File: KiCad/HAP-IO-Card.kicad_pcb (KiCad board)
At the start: 2 copper layers, 110 x 72 mm, 424 parts, among them CON601 AVR-JTAG-10, J201 TE_Connectivity_1-282834-0, J202 TE_Connectivity_282834-6, J203 GS3, J204 GS3, J205 GS3, J206 GS3, J207 GS3, J208 GS3, J209 GS3, J210 GS3, J211 TE_Connectivity_282834-6, J212 TE_Connectivity_1-282834-0, J401 TE_Connectivity_1-282834-0, J402 TE_Connectivity_282834-6, J501 TE_Connectivity_282834-3, J502 CONN_01X03_FEMALE, J601 ISP0, J602 ISP1, J603 CONN_01X02, J604 CONN_01X02, J605 CONN_01X02, J606 CONN_01X02, J607 CONN_01X03, J608 CONN_01X03, J701 5V_I/O_1, J702 5V_I/O_2, J703 NEO1, J704 NEO2, J705 NEO3, J706 NEO4, J707 CONN_01X03, Q201 ZXTN25050DFHTA, Q202 ZXTN25050DFHTA, Q203 ZXTN25050DFHTA, Q204 ZXTN25050DFHTA, Q205 ZXTN25050DFHTA, Q206 ZXTN25050DFHTA, Q207 ZXTN25050DFHTA, Q208 ZXTN25050DFHTA, U201 LTV-354T, U202 LTV-354T, U203 LTV-354T, U204 LTV-354T, U205 LTV-354T, U206 LTV-354T, U207 LTV-354T, U208 LTV-354T, U209 MCP23017, U401 ADS1115IDGST, U402 ADS1115IDGST, U501 LM1086-5V, U502 LM1086-3.3V, U701 TXB0102DCT

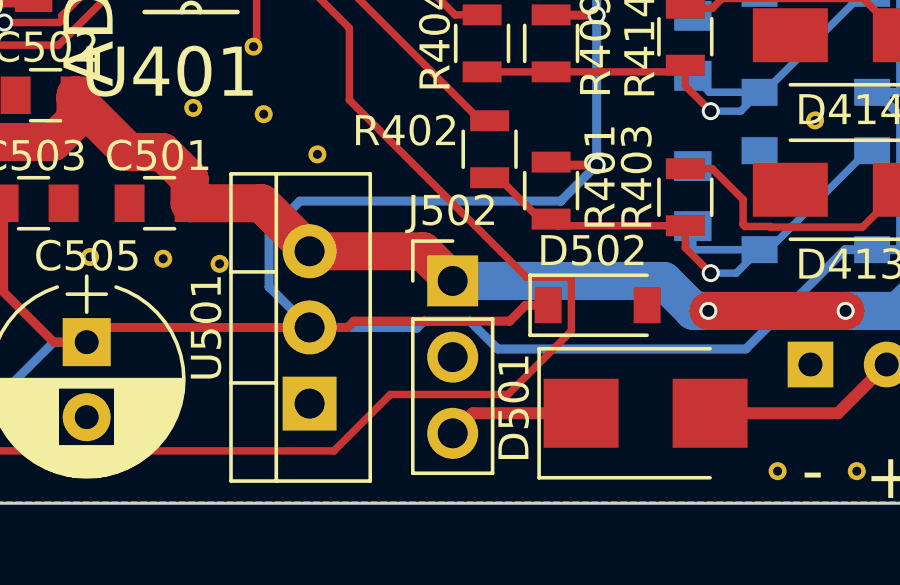
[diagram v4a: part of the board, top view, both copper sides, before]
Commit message: Updated EMI component
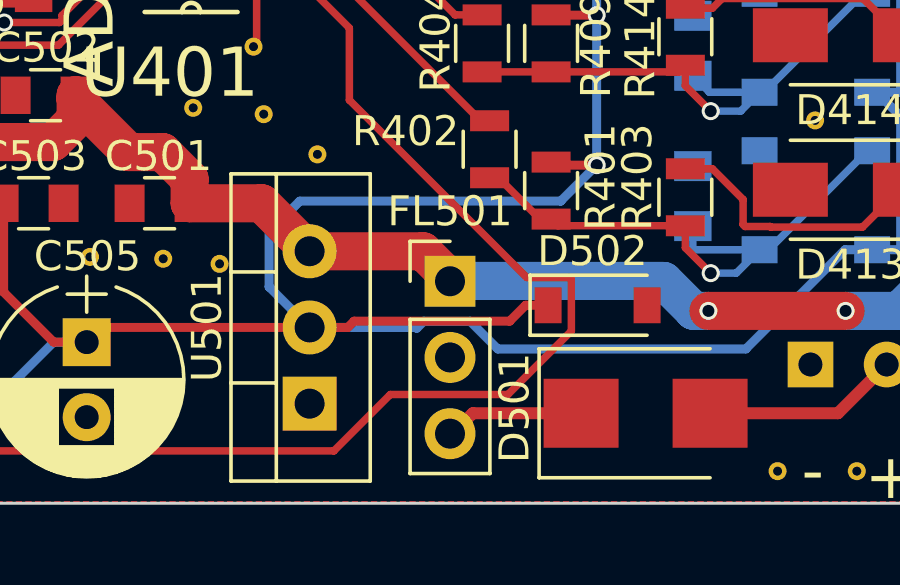
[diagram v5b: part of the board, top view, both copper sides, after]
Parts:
- removed J502: CONN_01X03_FEMALE, Pin_Headers:Pin_Header_Straight_1x03_Pitch2.54mm
- added FL501: EMI_Filter_LCL, Pin_Headers:Pin_Header_Straight_1x03_Pitch2.54mm, F.Cu at (119.9, 82.1)
- D501: value MBR340 -> MBRS360BT3G
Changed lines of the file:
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@@
     (add_net "/Sense Inputs/Sense8_DUT")
   )
+  (module Pin_Headers:Pin_Header_Straight_1x03_Pitch2.54mm (layer F.Cu)
+    (at 119.91 82.07)
+    (descr "Through hole straight pin header, 1x03, 2.54mm pitch, single row")
+    (tags "Through hole pin header THT 1x03 2.54mm single row")
+    (fp_text reference FL501 (at 0 -2.33) (layer F.SilkS)
+      (effects (font (size 1 1) (thickness 0.15)))
+    )
+    (fp_text value EMI_Filter_LCL (at 0 7.41) (layer F.Fab)
+      (effects (font (size 1 1) (thickness 0.15)))
+    )
+    (fp_text user %R (at 0 -2.33) (layer F.Fab)
+      (effects (font (size 1 1) (thickness 0.15)))
+    )
+    (fp_line (start 1.8 -1.8) (end -1.8 -1.8) (layer F.CrtYd) (width 0.05))
+    (fp_line (start 1.8 6.85) (end 1.8 -1.8) (layer F.CrtYd) (width 0.05))
+    (fp_line (start -1.8 6.85) (end 1.8 6.85) (layer F.CrtYd) (width 0.05))
+    (fp_line (start -1.8 -1.8) (end -1.8 6.85) (layer F.CrtYd) (width 0.05))
+    (fp_line (start -1.33 -1.33) (end 0 -1.33) (layer F.SilkS) (width 0.12))
+    (fp_line (start -1.33 0) (end -1.33 -1.33) (layer F.SilkS) (width 0.12))
+    (fp_line (start 1.33 1.27) (end -1.33 1.27) (layer F.SilkS) (width 0.12))
+    (fp_line (start 1.33 6.41) (end 1.33 1.27) (layer F.SilkS) (width 0.12))
+    (fp_line (start -1.33 6.41) (end 1.33 6.41) (layer F.SilkS) (width 0.12))
+    (fp_line (start -1.33 1.27) (end -1.33 6.41) (layer F.SilkS) (width 0.12))
+    (fp_line (start 1.27 -1.27) (end -1.27 -1.27) (layer F.Fab) (width 0.1))
+    (fp_line (start 1.27 6.35) (end 1.27 -1.27) (layer F.Fab) (width 0.1))
+    (fp_line (start -1.27 6.35) (end 1.27 6.35) (layer F.Fab) (width 0.1))
+    (fp_line (start -1.27 -1.27) (end -1.27 6.35) (layer F.Fab) (width 0.1))
+    (pad 3 thru_hole oval (at 0 5.08) (size 1.7 1.7) (drill 1) (layers *.Cu *.Mask)
+      (net 157 /Powersupply/12V_PWR2))
+    (pad 2 thru_hole oval (at 0 2.54) (size 1.7 1.7) (drill 1) (layers *.Cu *.Mask)
+      (net 94 Earth))
+    (pad 1 thru_hole rect (at 0 0) (size 1.7 1.7) (drill 1) (layers *.Cu *.Mask)
+      (net 107 +12V))
+    (model ${KISYS3DMOD}/Pin_Headers.3dshapes/Pin_Header_Straight_1x03_Pitch2.54mm.wrl
+      (at (xyz 0 -0.1 0))
+      (scale (xyz 1 1 1))
+      (rotate (xyz 0 0 90))
+    )
+  )
   (module Resistors_SMD:R_0805 (layer B.Cu)
     (at 87.67 86 270)
@@
       (effects (font (size 1 1) (thickness 0.15)))
     )
-    (fp_text value MBR340 (at 0 3.1) (layer F.Fab)
+    (fp_text value MBRS360BT3G (at 0 3.1) (layer F.Fab)
       (effects (font (size 1 1) (thickness 0.15)))
     )
@@
     (model ${KISYS3DMOD}/Pin_Headers.3dshapes/Pin_Header_Straight_1x03_Pitch2.54mm.wrl
       (at (xyz 0 -0.1 0))
-      (scale (xyz 1 1 1))
-      (rotate (xyz 0 0 90))
-    )
-  )
-  (module Pin_Headers:Pin_Header_Straight_1x03_Pitch2.54mm (layer F.Cu)
-    (at 120 82.06)
-    (descr "Through hole straight pin header, 1x03, 2.54mm pitch, single row")
-    (tags "Through hole pin header THT 1x03 2.54mm single row")
-    (fp_text reference J502 (at 0 -2.33) (layer F.SilkS)
-      (effects (font (size 1 1) (thickness 0.15)))
-    )
-    (fp_text value CONN_01X03_FEMALE (at 0 7.41) (layer F.Fab)
-      (effects (font (size 1 1) (thickness 0.15)))
-    )
-    (fp_text user %R (at 0 -2.33) (layer F.Fab)
-      (effects (font (size 1 1) (thickness 0.15)))
-    )
-    (fp_line (start 1.8 -1.8) (end -1.8 -1.8) (layer F.CrtYd) (width 0.05))
-    (fp_line (start 1.8 6.85) (end 1.8 -1.8) (layer F.CrtYd) (width 0.05))
-    (fp_line (start -1.8 6.85) (end 1.8 6.85) (layer F.CrtYd) (width 0.05))
-    (fp_line (start -1.8 -1.8) (end -1.8 6.85) (layer F.CrtYd) (width 0.05))
-    (fp_line (start -1.33 -1.33) (end 0 -1.33) (layer F.SilkS) (width 0.12))
-    (fp_line (start -1.33 0) (end -1.33 -1.33) (layer F.SilkS) (width 0.12))
-    (fp_line (start 1.33 1.27) (end -1.33 1.27) (layer F.SilkS) (width 0.12))
-    (fp_line (start 1.33 6.41) (end 1.33 1.27) (layer F.SilkS) (width 0.12))
-    (fp_line (start -1.33 6.41) (end 1.33 6.41) (layer F.SilkS) (width 0.12))
-    (fp_line (start -1.33 1.27) (end -1.33 6.41) (layer F.SilkS) (width 0.12))
-    (fp_line (start 1.27 -1.27) (end -1.27 -1.27) (layer F.Fab) (width 0.1))
-    (fp_line (start 1.27 6.35) (end 1.27 -1.27) (layer F.Fab) (width 0.1))
-    (fp_line (start -1.27 6.35) (end 1.27 6.35) (layer F.Fab) (width 0.1))
-    (fp_line (start -1.27 -1.27) (end -1.27 6.35) (layer F.Fab) (width 0.1))
-    (pad 3 thru_hole oval (at 0 5.08) (size 1.7 1.7) (drill 1) (layers *.Cu *.Mask)
-      (net 157 /Powersupply/12V_PWR2))
-    (pad 2 thru_hole oval (at 0 2.54) (size 1.7 1.7) (drill 1) (layers *.Cu *.Mask)
-      (net 94 Earth))
-    (pad 1 thru_hole rect (at 0 0) (size 1.7 1.7) (drill 1) (layers *.Cu *.Mask)
-      (net 107 +12V))
-    (model ${KISYS3DMOD}/Pin_Headers.3dshapes/Pin_Header_Straight_1x03_Pitch2.54mm.wrl
-      (at (xyz 0 -0.1 0))
